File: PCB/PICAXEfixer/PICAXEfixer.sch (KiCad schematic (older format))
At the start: 7 parts, among them J1 Conn_01x03, J2 Conn_01x02, J3 Conn_01x04, Q1 2N7000, U1 PICAXEM2

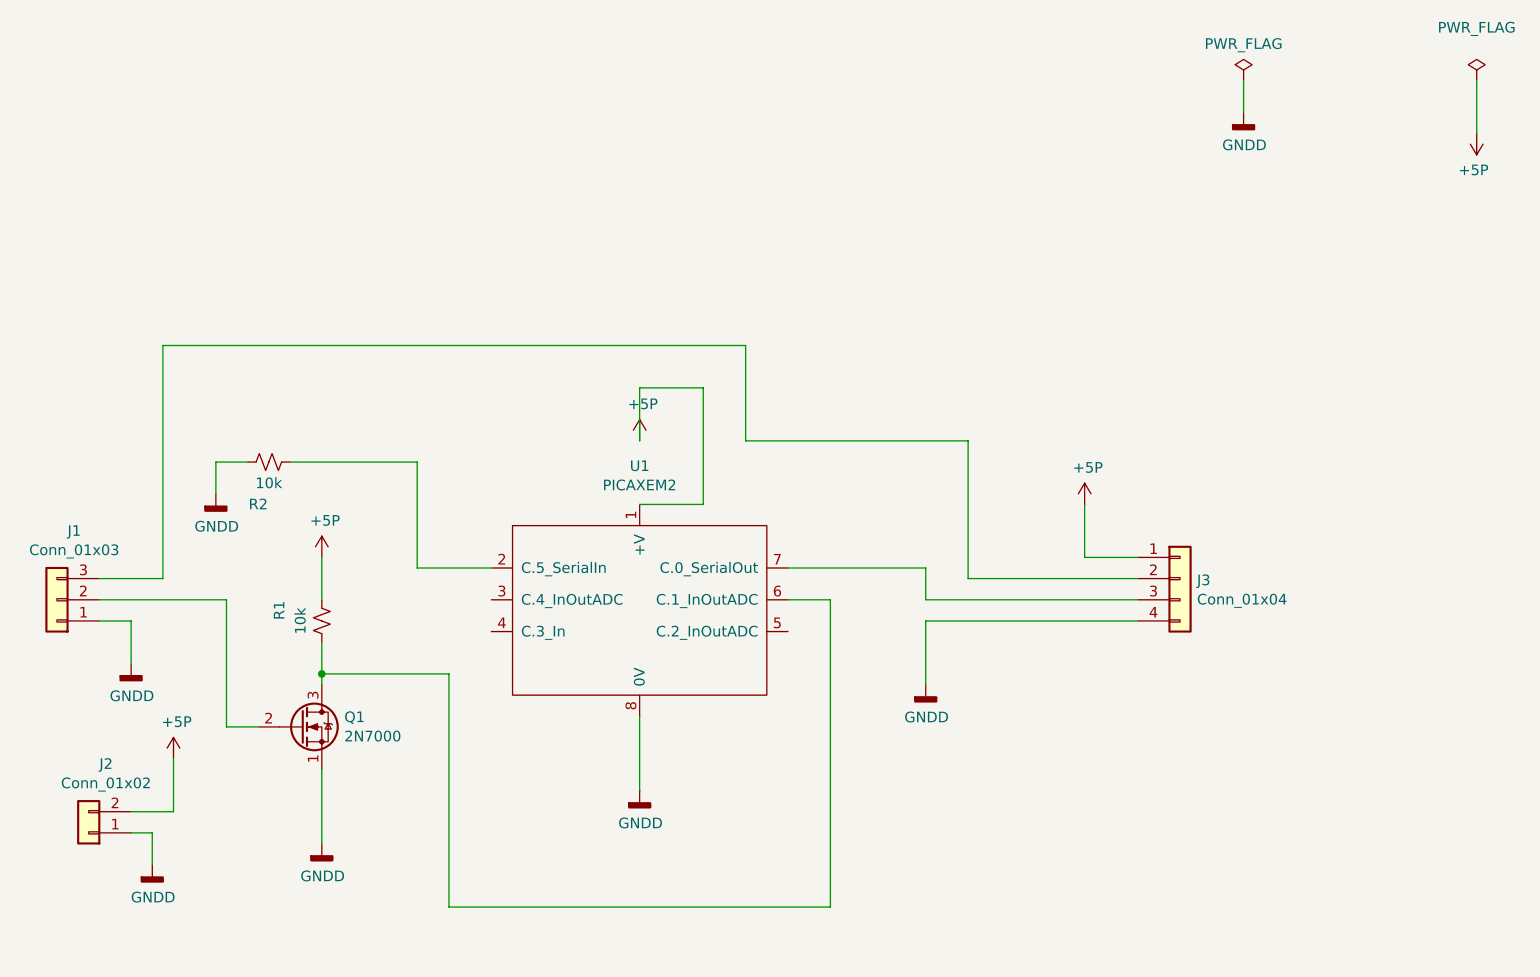
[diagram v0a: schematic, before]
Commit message: Code and circuit tested; works.
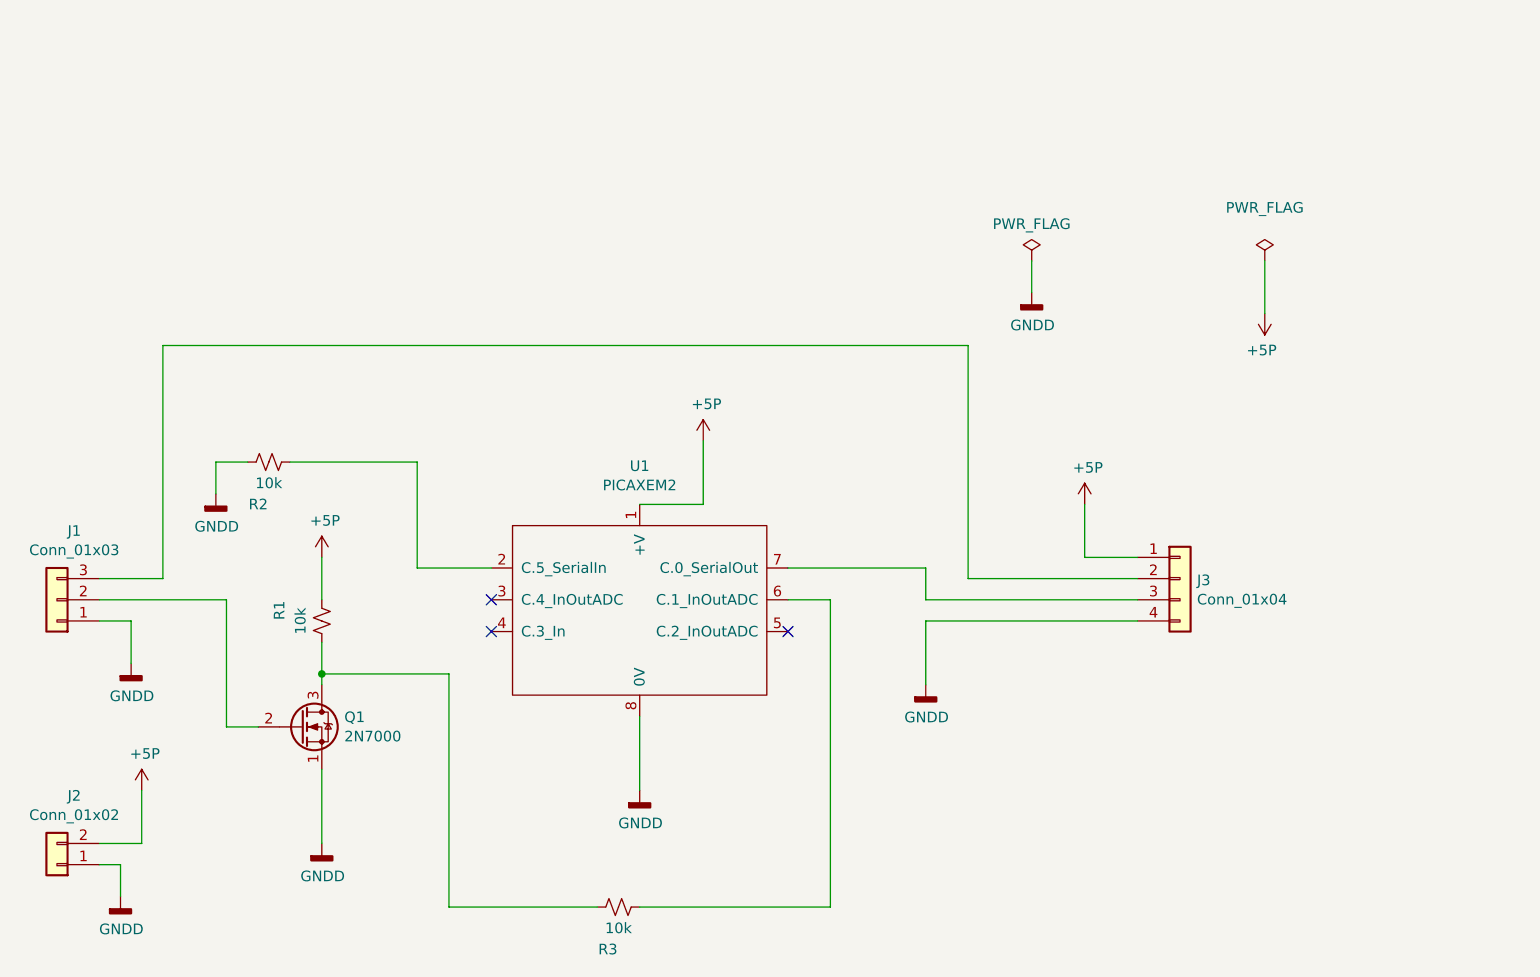
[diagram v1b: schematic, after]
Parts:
- added R3: 10k, Resistor_THT:R_Axial_DIN0922_L20.0mm_D9.0mm_P25.40mm_Horizontal, symbol Device:R_Small_US
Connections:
- net at Q1.3 (D), R1.1: now also R3.2; no longer U1.6 (C.1_InOutADC)
- new net: R3.1, U1.6 (C.1_InOutADC)
- no-connect marks 0 -> 3
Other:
- moved on the sheet: J2
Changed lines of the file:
@@
 Comment4 ""
 $EndDescr
-Wire Wire Line
-	5950 2750 5950 2500
 $Comp
 L power:GNDD #PWR05
@@
 L power:PWR_FLAG #FLG0101
 U 1 1 5DE94C52
-P 8800 1050
-F 0 "#FLG0101" H 8800 1125 50  0001 C CNN
-F 1 "PWR_FLAG" H 8800 1223 50  0000 C CNN
-F 2 "" H 8800 1050 50  0001 C CNN
-F 3 "~" H 8800 1050 50  0001 C CNN
-	1    8800 1050
+P 7800 1900
+F 0 "#FLG0101" H 7800 1975 50  0001 C CNN
+F 1 "PWR_FLAG" H 7800 2073 50  0000 C CNN
+F 2 "" H 7800 1900 50  0001 C CNN
+F 3 "~" H 7800 1900 50  0001 C CNN
+	1    7800 1900
 	1    0    0    -1
 $EndComp
@@
 L power:PWR_FLAG #FLG0104
 U 1 1 5DE95686
-P 9900 1050
-F 0 "#FLG0104" H 9900 1125 50  0001 C CNN
-F 1 "PWR_FLAG" H 9900 1300 50  0000 C CNN
-F 2 "" H 9900 1050 50  0001 C CNN
-F 3 "~" H 9900 1050 50  0001 C CNN
-	1    9900 1050
+P 8900 1900
+F 0 "#FLG0104" H 8900 1975 50  0001 C CNN
+F 1 "PWR_FLAG" H 8900 2150 50  0000 C CNN
+F 2 "" H 8900 1900 50  0001 C CNN
+F 3 "~" H 8900 1900 50  0001 C CNN
+	1    8900 1900
 	1    0    0    -1
 $EndComp
@@
 L power:GNDD #PWR0101
 U 1 1 5DE95977
-P 8800 1200
-F 0 "#PWR0101" H 8800 950 50  0001 C CNN
-F 1 "GNDD" H 8804 1045 50  0000 C CNN
-F 2 "" H 8800 1200 50  0001 C CNN
-F 3 "" H 8800 1200 50  0001 C CNN
-	1    8800 1200
+P 7800 2050
+F 0 "#PWR0101" H 7800 1800 50  0001 C CNN
+F 1 "GNDD" H 7804 1895 50  0000 C CNN
+F 2 "" H 7800 2050 50  0001 C CNN
+F 3 "" H 7800 2050 50  0001 C CNN
+	1    7800 2050
 	1    0    0    -1
 $EndComp
@@
 L power:+5P #PWR0104
 U 1 1 5DE96AE6
-P 9900 1300
-F 0 "#PWR0104" H 9900 1150 50  0001 C CNN
-F 1 "+5P" H 9915 1473 50  0000 C CNN
-F 2 "" H 9900 1300 50  0001 C CNN
-F 3 "" H 9900 1300 50  0001 C CNN
-	1    9900 1300
+P 8900 2150
+F 0 "#PWR0104" H 8900 2000 50  0001 C CNN
+F 1 "+5P" H 8915 2323 50  0000 C CNN
+F 2 "" H 8900 2150 50  0001 C CNN
+F 3 "" H 8900 2150 50  0001 C CNN
+	1    8900 2150
 	-1   0    0    1
 $EndComp
 Wire Wire Line
-	9900 1050 9900 1300
+	8900 1900 8900 2150
 $Comp
 L PICAXE:PICAXEM2 U1
@@
 Wire Wire Line
 	5950 4050 5950 4400
-Wire Wire Line
-	5950 2500 6250 2500
-Wire Wire Line
-	6250 2500 6250 3050
 Wire Wire Line
 	6250 3050 5950 3050
@@
 $EndComp
 $Comp
-L power:GNDD #PWR?
-U 1 1 6174521D
-P 3650 4750
-F 0 "#PWR?" H 3650 4500 50  0001 C CNN
-F 1 "GNDD" H 3654 4595 50  0000 C CNN
-F 2 "" H 3650 4750 50  0001 C CNN
-F 3 "" H 3650 4750 50  0001 C CNN
-	1    3650 4750
-	1    0    0    -1
-$EndComp
-$Comp
-L Connector_Generic:Conn_01x02 J2
-U 1 1 617470D3
-P 3350 4600
-F 0 "J2" H 3268 4275 50  0000 C CNN
-F 1 "Conn_01x02" H 3268 4366 50  0000 C CNN
-F 2 "" H 3350 4600 50  0001 C CNN
-F 3 "~" H 3350 4600 50  0001 C CNN
-	1    3350 4600
-	-1   0    0    1
-$EndComp
-$Comp
 L Transistor_FET:2N7000 Q1
 U 1 1 6174AC5A
@@
 	4900 2850 4900 3350
 $Comp
-L power:GNDD #PWR?
+L power:GNDD #PWR0102
 U 1 1 61754125
 P 3550 3800
-F 0 "#PWR?" H 3550 3550 50  0001 C CNN
+F 0 "#PWR0102" H 3550 3550 50  0001 C CNN
 F 1 "GNDD" H 3554 3645 50  0000 C CNN
 F 2 "" H 3550 3800 50  0001 C CNN
@@
 $EndComp
 $Comp
-L power:GNDD #PWR?
+L power:GNDD #PWR0103
 U 1 1 61754A38
 P 7300 3900
-F 0 "#PWR?" H 7300 3650 50  0001 C CNN
+F 0 "#PWR0103" H 7300 3650 50  0001 C CNN
 F 1 "GNDD" H 7304 3745 50  0000 C CNN
 F 2 "" H 7300 3900 50  0001 C CNN
 F 3 "" H 7300 3900 50  0001 C CNN
 	1    7300 3900
-	1    0    0    -1
-$EndComp
-$Comp
-L power:+5P #PWR?
-U 1 1 6175513A
-P 3750 4250
-F 0 "#PWR?" H 3750 4100 50  0001 C CNN
-F 1 "+5P" H 3765 4423 50  0000 C CNN
-F 2 "" H 3750 4250 50  0001 C CNN
-F 3 "" H 3750 4250 50  0001 C CNN
-	1    3750 4250
 	1    0    0    -1
 $EndComp
@@
 $EndComp
 $Comp
-L power:+5P #PWR?
+L power:+5P #PWR0105
 U 1 1 6175652D
 P 8050 3050
-F 0 "#PWR?" H 8050 2900 50  0001 C CNN
+F 0 "#PWR0105" H 8050 2900 50  0001 C CNN
 F 1 "+5P" H 8065 3223 50  0000 C CNN
 F 2 "" H 8050 3050 50  0001 C CNN
@@
 	3550 3600 3400 3600
 Wire Wire Line
-	3550 4600 3650 4600
-Wire Wire Line
-	3650 4600 3650 4750
-Wire Wire Line
-	3550 4500 3750 4500
-Wire Wire Line
-	3750 4500 3750 4250
-Wire Wire Line
 	8300 3600 7300 3600
 Wire Wire Line
@@
 	8050 3300 8050 3050
 $Comp
-L power:GNDD #PWR?
+L power:GNDD #PWR0106
 U 1 1 6175F7C3
 P 4450 4650
-F 0 "#PWR?" H 4450 4400 50  0001 C CNN
+F 0 "#PWR0106" H 4450 4400 50  0001 C CNN
 F 1 "GNDD" H 4454 4495 50  0000 C CNN
 F 2 "" H 4450 4650 50  0001 C CNN
@@
 $EndComp
 $Comp
-L power:+5P #PWR?
+L power:+5P #PWR0107
 U 1 1 6175FF0E
 P 4450 3300
-F 0 "#PWR?" H 4450 3150 50  0001 C CNN
+F 0 "#PWR0107" H 4450 3150 50  0001 C CNN
 F 1 "+5P" H 4465 3473 50  0000 C CNN
 F 2 "" H 4450 3300 50  0001 C CNN
@@
 $EndComp
 Wire Wire Line
-	3400 3500 4000 3500
-Wire Wire Line
-	4000 3500 4000 4100
-Wire Wire Line
-	4000 4100 4150 4100
-Wire Wire Line
 	4450 4300 4450 4650
 Wire Wire Line
@@
 Wire Wire Line
 	6850 3500 6850 4950
-Wire Wire Line
-	6850 4950 5050 4950
 Wire Wire Line
 	5050 4950 5050 3850
@@
 	8300 3400 7500 3400
 Wire Wire Line
-	7500 3400 7500 2750
-Wire Wire Line
-	7500 2750 6450 2750
-Wire Wire Line
-	6450 2750 6450 2300
-Wire Wire Line
-	6450 2300 3700 2300
-Wire Wire Line
 	3700 2300 3700 3400
 Wire Wire Line
@@
 L power:+5P #PWR06
 U 1 1 5DE6DFB6
-P 5950 2750
-F 0 "#PWR06" H 5950 2600 50  0001 C CNN
-F 1 "+5P" H 5965 2923 50  0000 C CNN
-F 2 "" H 5950 2750 50  0001 C CNN
-F 3 "" H 5950 2750 50  0001 C CNN
-	1    5950 2750
+P 6250 2750
+F 0 "#PWR06" H 6250 2600 50  0001 C CNN
+F 1 "+5P" H 6265 2923 50  0000 C CNN
+F 2 "" H 6250 2750 50  0001 C CNN
+F 3 "" H 6250 2750 50  0001 C CNN
+	1    6250 2750
 	1    0    0    -1
 $EndComp
@@
 	4300 2850 4900 2850
 Wire Wire Line
-	8800 1050 8800 1200
+	7800 1900 7800 2050
+$Comp
+L Device:R_Small_US R3
+U 1 1 61769851
+P 5850 4950
+F 0 "R3" V 6050 4900 50  0000 C CNN
+F 1 "10k" V 5950 4950 50  0000 C CNN
+F 2 "Resistor_THT:R_Axial_DIN0922_L20.0mm_D9.0mm_P25.40mm_Horizontal" H 5850 4950 50  0001 C CNN
+F 3 "~" H 5850 4950 50  0001 C CNN
+	1    5850 4950
+	0    1    1    0
+$EndComp
+Wire Wire Line
+	5050 4950 5750 4950
+Wire Wire Line
+	5950 4950 6850 4950
+Wire Wire Line
+	3400 3500 4000 3500
+Wire Wire Line
+	4000 4100 4150 4100
+Wire Wire Line
+	4000 3500 4000 4100
+Wire Wire Line
+	3600 4650 3600 4400
+Wire Wire Line
+	3400 4650 3600 4650
+Wire Wire Line
+	3500 4750 3500 4900
+Wire Wire Line
+	3400 4750 3500 4750
+$Comp
+L power:+5P #PWR0108
+U 1 1 6175513A
+P 3600 4400
+F 0 "#PWR0108" H 3600 4250 50  0001 C CNN
+F 1 "+5P" H 3615 4573 50  0000 C CNN
+F 2 "" H 3600 4400 50  0001 C CNN
+F 3 "" H 3600 4400 50  0001 C CNN
+	1    3600 4400
+	1    0    0    -1
+$EndComp
+$Comp
+L Connector_Generic:Conn_01x02 J2
+U 1 1 617470D3
+P 3200 4750
+F 0 "J2" H 3118 4425 50  0000 C CNN
+F 1 "Conn_01x02" H 3118 4516 50  0000 C CNN
+F 2 "" H 3200 4750 50  0001 C CNN
+F 3 "~" H 3200 4750 50  0001 C CNN
+	1    3200 4750
+	-1   0    0    1
+$EndComp
+$Comp
+L power:GNDD #PWR0109
+U 1 1 6174521D
+P 3500 4900
+F 0 "#PWR0109" H 3500 4650 50  0001 C CNN
+F 1 "GNDD" H 3504 4745 50  0000 C CNN
+F 2 "" H 3500 4900 50  0001 C CNN
+F 3 "" H 3500 4900 50  0001 C CNN
+	1    3500 4900
+	1    0    0    -1
+$EndComp
+Wire Wire Line
+	7500 3400 7500 2300
+Wire Wire Line
+	3700 2300 7500 2300
+Wire Wire Line
+	6250 2750 6250 3050
+NoConn ~ 5250 3650
+NoConn ~ 6650 3650
+NoConn ~ 5250 3500
 $EndSCHEMATC

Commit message: pcb laying out
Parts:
- J1: footprint (none) -> Connector_PinHeader_2.54mm:PinHeader_1x03_P2.54mm_Vertical
- J2: footprint (none) -> Connector_BarrelJack:BarrelJack_Wuerth_6941xx301002
- J3: footprint (none) -> Connector_PinHeader_2.54mm:PinHeader_1x04_P2.54mm_Vertical
- U1: footprint (none) -> Package_DIP:DIP-8_W7.62mm
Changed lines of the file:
@@
 F 0 "U1" H 5950 3031 50  0000 C CNN
 F 1 "PICAXEM2" H 5950 2940 50  0000 C CNN
-F 2 "" H 5950 2950 50  0001 C CNN
+F 2 "Package_DIP:DIP-8_W7.62mm" H 5950 2950 50  0001 C CNN
 F 3 "" H 5950 2950 50  0001 C CNN
 	1    5950 2950
@@
 F 0 "J1" H 3118 3175 50  0000 C CNN
 F 1 "Conn_01x03" H 3118 3266 50  0000 C CNN
-F 2 "" H 3200 3500 50  0001 C CNN
+F 2 "Connector_PinHeader_2.54mm:PinHeader_1x03_P2.54mm_Vertical" H 3200 3500 50  0001 C CNN
 F 3 "~" H 3200 3500 50  0001 C CNN
 	1    3200 3500
@@
 F 0 "J3" H 8580 3392 50  0000 L CNN
 F 1 "Conn_01x04" H 8580 3301 50  0000 L CNN
-F 2 "" H 8500 3400 50  0001 C CNN
+F 2 "Connector_PinHeader_2.54mm:PinHeader_1x04_P2.54mm_Vertical" H 8500 3400 50  0001 C CNN
 F 3 "~" H 8500 3400 50  0001 C CNN
 	1    8500 3400
@@
 F 0 "J2" H 3118 4425 50  0000 C CNN
 F 1 "Conn_01x02" H 3118 4516 50  0000 C CNN
-F 2 "" H 3200 4750 50  0001 C CNN
+F 2 "Connector_BarrelJack:BarrelJack_Wuerth_6941xx301002" H 3200 4750 50  0001 C CNN
 F 3 "~" H 3200 4750 50  0001 C CNN
 	1    3200 4750

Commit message: PCB laid out
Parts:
- added C1: 100uF, Capacitor_THT:CP_Radial_D10.0mm_P5.00mm, symbol Device:CP
- added C2: 100nF, Capacitor_THT:C_Disc_D4.3mm_W1.9mm_P5.00mm, symbol Device:C_Small
- added R4: 10k, Resistor_THT:R_Axial_DIN0309_L9.0mm_D3.2mm_P15.24mm_Horizontal, symbol Device:R_Small_US
- R1, R2, R3: footprint Resistor_THT:R_Axial_DIN0922_L20.0mm_D9.0mm_P25.40mm_Horizontal -> Resistor_THT:R_Axial_DIN0309_L9.0mm_D3.2mm_P15.24mm_Horizontal
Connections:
- net +5P: now also C1.1, C2.1
- net GNDD: now also C1.2, C2.2
- net at U1.7 (C.0_SerialOut): now also R4.2; no longer J3.3 (Pin_3)
- new net: J3.3 (Pin_3), R4.1
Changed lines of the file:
@@
 EESchema Schematic File Version 4
+LIBS:PICAXEfixer-cache
 EELAYER 30 0
 EELAYER END
@@
 F 0 "R2" V 4400 2800 50  0000 C CNN
 F 1 "10k" V 4300 2850 50  0000 C CNN
-F 2 "Resistor_THT:R_Axial_DIN0922_L20.0mm_D9.0mm_P25.40mm_Horizontal" H 4200 2850 50  0001 C CNN
+F 2 "Resistor_THT:R_Axial_DIN0309_L9.0mm_D3.2mm_P15.24mm_Horizontal" H 4200 2850 50  0001 C CNN
 F 3 "~" H 4200 2850 50  0001 C CNN
 	1    4200 2850
@@
 $EndComp
 Wire Wire Line
-	5950 4050 5950 4400
+	5950 4050 5950 4200
 Wire Wire Line
 	6250 3050 5950 3050
@@
 F 0 "R1" V 4650 3550 50  0000 C CNN
 F 1 "10k" V 4550 3600 50  0000 C CNN
-F 2 "Resistor_THT:R_Axial_DIN0922_L20.0mm_D9.0mm_P25.40mm_Horizontal" H 4450 3600 50  0001 C CNN
+F 2 "Resistor_THT:R_Axial_DIN0309_L9.0mm_D3.2mm_P15.24mm_Horizontal" H 4450 3600 50  0001 C CNN
 F 3 "~" H 4450 3600 50  0001 C CNN
 	1    4450 3600
@@
 Wire Wire Line
 	4450 3850 4450 3900
-Wire Wire Line
-	6650 3350 7300 3350
 Wire Wire Line
 	7300 3350 7300 3500
@@
 F 0 "R3" V 6050 4900 50  0000 C CNN
 F 1 "10k" V 5950 4950 50  0000 C CNN
-F 2 "Resistor_THT:R_Axial_DIN0922_L20.0mm_D9.0mm_P25.40mm_Horizontal" H 5850 4950 50  0001 C CNN
+F 2 "Resistor_THT:R_Axial_DIN0309_L9.0mm_D3.2mm_P15.24mm_Horizontal" H 5850 4950 50  0001 C CNN
 F 3 "~" H 5850 4950 50  0001 C CNN
 	1    5850 4950
@@
 	4000 3500 4000 4100
 Wire Wire Line
-	3600 4650 3600 4400
+	3600 4650 3600 4550
 Wire Wire Line
 	3400 4650 3600 4650
 Wire Wire Line
-	3500 4750 3500 4900
+	3500 4750 3500 4850
 Wire Wire Line
 	3400 4750 3500 4750
@@
 NoConn ~ 6650 3650
 NoConn ~ 5250 3500
+$Comp
+L Device:R_Small_US R4
+U 1 1 6177EB51
+P 7150 3350
+F 0 "R4" V 7350 3300 50  0000 C CNN
+F 1 "10k" V 7250 3350 50  0000 C CNN
+F 2 "Resistor_THT:R_Axial_DIN0309_L9.0mm_D3.2mm_P15.24mm_Horizontal" H 7150 3350 50  0001 C CNN
+F 3 "~" H 7150 3350 50  0001 C CNN
+	1    7150 3350
+	0    1    1    0
+$EndComp
+Wire Wire Line
+	7250 3350 7300 3350
+Wire Wire Line
+	6650 3350 7050 3350
+$Comp
+L Device:C_Small C2
+U 1 1 61781CDD
+P 6300 4200
+F 0 "C2" V 6071 4200 50  0000 C CNN
+F 1 "100nF" V 6162 4200 50  0000 C CNN
+F 2 "Capacitor_THT:C_Disc_D4.3mm_W1.9mm_P5.00mm" H 6300 4200 50  0001 C CNN
+F 3 "~" H 6300 4200 50  0001 C CNN
+	1    6300 4200
+	0    1    1    0
+$EndComp
+$Comp
+L Device:CP C1
+U 1 1 617830B4
+P 3850 4700
+F 0 "C1" H 3968 4746 50  0000 L CNN
+F 1 "100uF" H 3968 4655 50  0000 L CNN
+F 2 "Capacitor_THT:CP_Radial_D10.0mm_P5.00mm" H 3888 4550 50  0001 C CNN
+F 3 "~" H 3850 4700 50  0001 C CNN
+	1    3850 4700
+	1    0    0    -1
+$EndComp
+Wire Wire Line
+	3500 4850 3850 4850
+Connection ~ 3500 4850
+Wire Wire Line
+	3500 4850 3500 4900
+Wire Wire Line
+	3850 4550 3600 4550
+Connection ~ 3600 4550
+Wire Wire Line
+	3600 4550 3600 4400
+Wire Wire Line
+	6200 4200 5950 4200
+Connection ~ 5950 4200
+Wire Wire Line
+	5950 4200 5950 4400
+Wire Wire Line
+	6400 4200 6750 4200
+Wire Wire Line
+	6750 4200 6750 3050
+Wire Wire Line
+	6750 3050 6250 3050
+Connection ~ 6250 3050
 $EndSCHEMATC

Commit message: final
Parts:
- C1: footprint Capacitor_THT:CP_Radial_D10.0mm_P5.00mm -> Capacitor_THT:CP_Radial_D10.0mm_P7.50mm
- C2: footprint Capacitor_THT:C_Disc_D4.3mm_W1.9mm_P5.00mm -> Capacitor_THT:C_Disc_D7.5mm_W5.0mm_P10.00mm
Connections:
- net +5P: now also J2.1 (Pin_1); no longer J2.2 (Pin_2)
- net GNDD: now also J2.2 (Pin_2); no longer J2.1 (Pin_1)
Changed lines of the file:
@@
 EESchema Schematic File Version 4
-LIBS:PICAXEfixer-cache
 EELAYER 30 0
 EELAYER END
@@
 Wire Wire Line
 	4000 3500 4000 4100
-Wire Wire Line
-	3600 4650 3600 4550
-Wire Wire Line
-	3400 4650 3600 4650
-Wire Wire Line
-	3500 4750 3500 4850
-Wire Wire Line
-	3400 4750 3500 4750
 $Comp
 L power:+5P #PWR0108
@@
 F 0 "C2" V 6071 4200 50  0000 C CNN
 F 1 "100nF" V 6162 4200 50  0000 C CNN
-F 2 "Capacitor_THT:C_Disc_D4.3mm_W1.9mm_P5.00mm" H 6300 4200 50  0001 C CNN
+F 2 "Capacitor_THT:C_Disc_D7.5mm_W5.0mm_P10.00mm" H 6300 4200 50  0001 C CNN
 F 3 "~" H 6300 4200 50  0001 C CNN
 	1    6300 4200
@@
 F 0 "C1" H 3968 4746 50  0000 L CNN
 F 1 "100uF" H 3968 4655 50  0000 L CNN
-F 2 "Capacitor_THT:CP_Radial_D10.0mm_P5.00mm" H 3888 4550 50  0001 C CNN
+F 2 "Capacitor_THT:CP_Radial_D10.0mm_P7.50mm" H 3888 4550 50  0001 C CNN
 F 3 "~" H 3850 4700 50  0001 C CNN
 	1    3850 4700
@@
 	6750 3050 6250 3050
 Connection ~ 6250 3050
+Wire Wire Line
+	3400 4650 3500 4650
+Wire Wire Line
+	3500 4650 3500 4850
+Wire Wire Line
+	3400 4750 3600 4750
+Wire Wire Line
+	3600 4550 3600 4750
 $EndSCHEMATC

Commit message: Circuit built & testing, functions erratically :/
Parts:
- added J4: Jumper, Connector_PinHeader_2.54mm:PinHeader_1x02_P2.54mm_Vertical, symbol Connector:Conn_01x02_Male
- J1: value Conn_01x03 -> From PC
- J2: value Conn_01x02 -> Power
- J3: value Conn_01x04 -> To PICAXE
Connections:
- net GNDD: now also J4.2 (Pin_2)
- net at U1.4 (C.3_In): now also J4.1 (Pin_1)
- no-connect marks 3 -> 2
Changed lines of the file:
@@
 P 3200 3500
 F 0 "J1" H 3118 3175 50  0000 C CNN
-F 1 "Conn_01x03" H 3118 3266 50  0000 C CNN
+F 1 "From PC" H 3118 3266 50  0000 C CNN
 F 2 "Connector_PinHeader_2.54mm:PinHeader_1x03_P2.54mm_Vertical" H 3200 3500 50  0001 C CNN
 F 3 "~" H 3200 3500 50  0001 C CNN
@@
 P 8500 3400
 F 0 "J3" H 8580 3392 50  0000 L CNN
-F 1 "Conn_01x04" H 8580 3301 50  0000 L CNN
+F 1 "To PICAXE" H 8580 3301 50  0000 L CNN
 F 2 "Connector_PinHeader_2.54mm:PinHeader_1x04_P2.54mm_Vertical" H 8500 3400 50  0001 C CNN
 F 3 "~" H 8500 3400 50  0001 C CNN
@@
 	6850 3500 6850 4950
 Wire Wire Line
-	5050 4950 5050 3850
-Wire Wire Line
-	5050 3850 4450 3850
+	4900 4950 4900 3850
+Wire Wire Line
+	4900 3850 4450 3850
 Connection ~ 4450 3850
 Wire Wire Line
@@
 $EndComp
 Wire Wire Line
-	5050 4950 5750 4950
+	4900 4950 5750 4950
 Wire Wire Line
 	5950 4950 6850 4950
@@
 P 3200 4750
 F 0 "J2" H 3118 4425 50  0000 C CNN
-F 1 "Conn_01x02" H 3118 4516 50  0000 C CNN
+F 1 "Power" H 3118 4516 50  0000 C CNN
 F 2 "Connector_BarrelJack:BarrelJack_Wuerth_6941xx301002" H 3200 4750 50  0001 C CNN
 F 3 "~" H 3200 4750 50  0001 C CNN
@@
 Wire Wire Line
 	6250 2750 6250 3050
-NoConn ~ 5250 3650
 NoConn ~ 6650 3650
 NoConn ~ 5250 3500
@@
 Wire Wire Line
 	3600 4550 3600 4750
+$Comp
+L power:GNDD #PWR0110
+U 1 1 61A238E2
+P 5100 4075
+F 0 "#PWR0110" H 5100 3825 50  0001 C CNN
+F 1 "GNDD" H 5104 3920 50  0000 C CNN
+F 2 "" H 5100 4075 50  0001 C CNN
+F 3 "" H 5100 4075 50  0001 C CNN
+	1    5100 4075
+	1    0    0    -1
+$EndComp
+$Comp
+L Connector:Conn_01x02_Male J4
+U 1 1 61A247ED
+P 4900 3650
+F 0 "J4" H 5008 3831 50  0000 C CNN
+F 1 "Jumper" H 5008 3740 50  0000 C CNN
+F 2 "Connector_PinHeader_2.54mm:PinHeader_1x02_P2.54mm_Vertical" H 4900 3650 50  0001 C CNN
+F 3 "~" H 4900 3650 50  0001 C CNN
+	1    4900 3650
+	1    0    0    -1
+$EndComp
+Wire Wire Line
+	5250 3650 5100 3650
+Wire Wire Line
+	5100 3750 5100 4075
 $EndSCHEMATC
